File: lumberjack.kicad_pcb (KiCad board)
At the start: 2 copper layers, 285.4 x 94.9 mm, 151 parts, among them J1 USB_OTG, J2 AVR_ISP_6, SW1 RESET, SW2 BOOT, U1 ATMEGA328-PU, Y1 16MHz

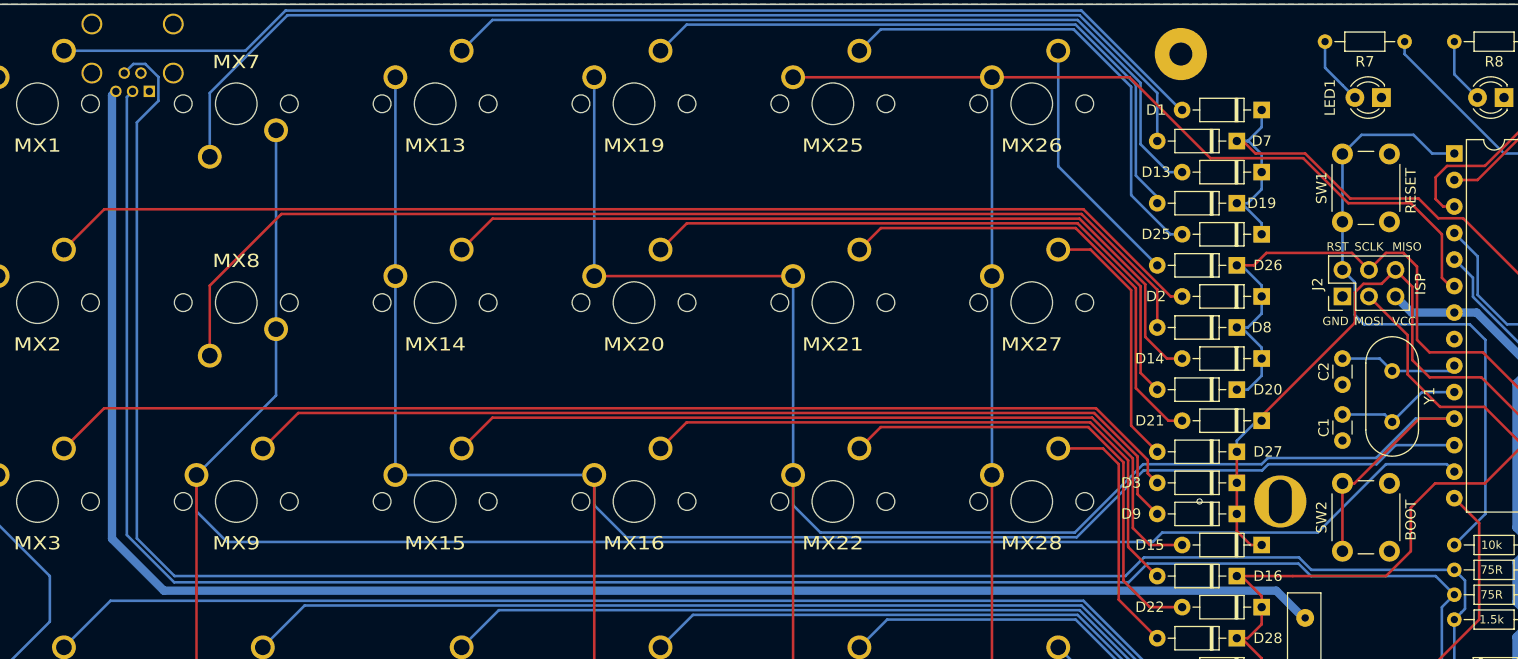
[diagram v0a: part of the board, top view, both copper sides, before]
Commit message: Add JST socket footprint for USB daughterboard
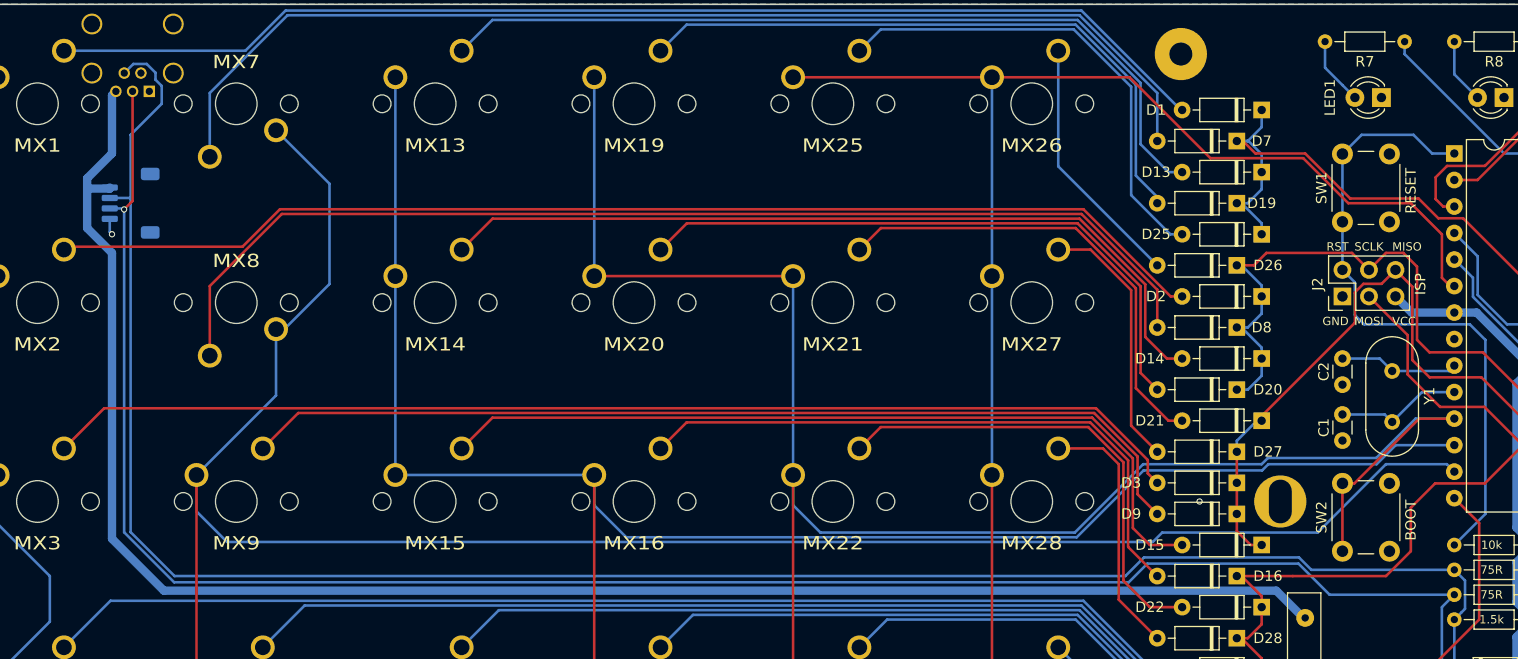
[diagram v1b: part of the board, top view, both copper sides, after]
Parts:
- added J3: JST, Connector_JST:JST_SH_SM04B-SRSS-TB_1x04-1MP_P1.00mm_Horizontal, B.Cu at (28.0, 73.8)
- added REF**: OSHW-Logo2_9.8x8mm_Copper, Symbol:OSHW-Logo2_9.8x8mm_Copper, B.Cu at (147.6, 116.1)
- J1: value USB_OTG -> USB
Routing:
- net /COL1: track 221.9 -> 226.6 mm
- net Net-(F1-Pad1): track 160.5 -> 164.8 mm
- net Net-(D67-Pad1): track 188.6 -> 191.4 mm
- net Net-(D66-Pad1): track 185.0 -> 186.6 mm, vias 0 -> 1
- net GND: track 0.00 -> 1.57 mm, vias 3 -> 4
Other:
- rule pad_to_mask_clearance: 0.2 -> 0
- board text added: "Lumberjack rev1.2 u/peejeh 01/2021"
- board text removed: "Lumberjack rev1.1 u/peejeh 12/2020"

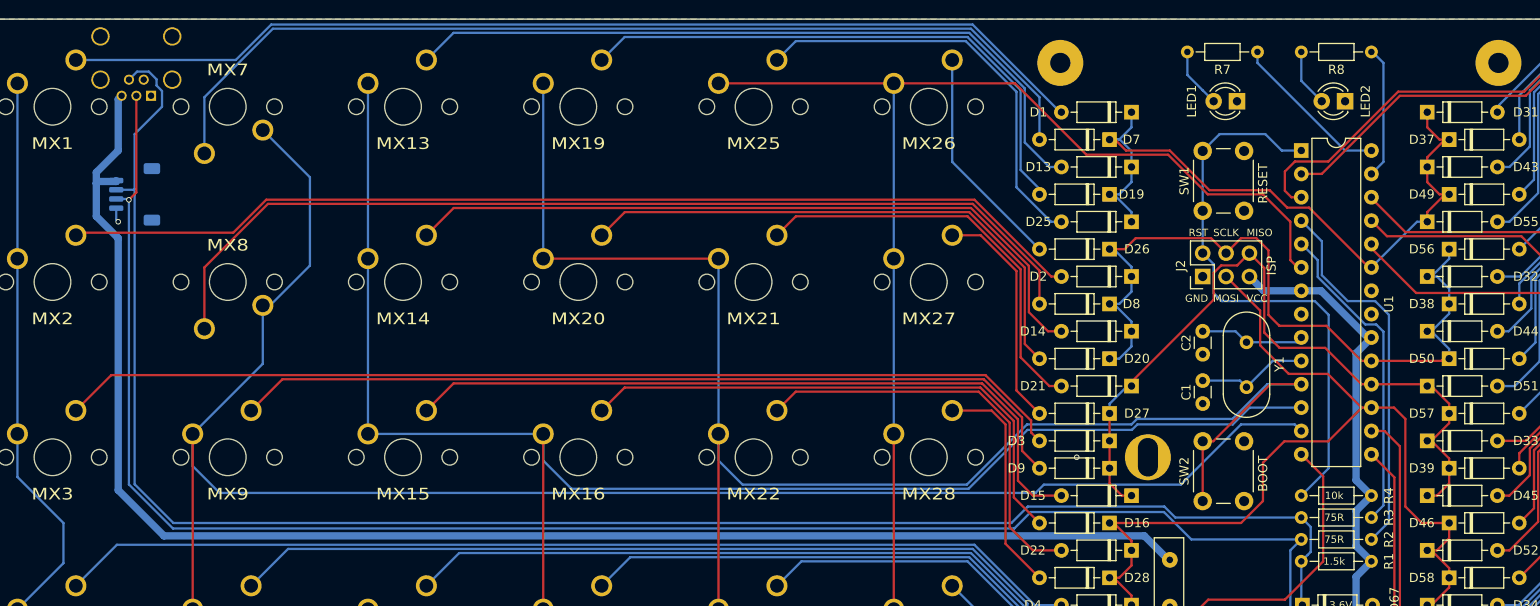
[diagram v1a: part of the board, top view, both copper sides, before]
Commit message: Add optional USB-C connector and resistors
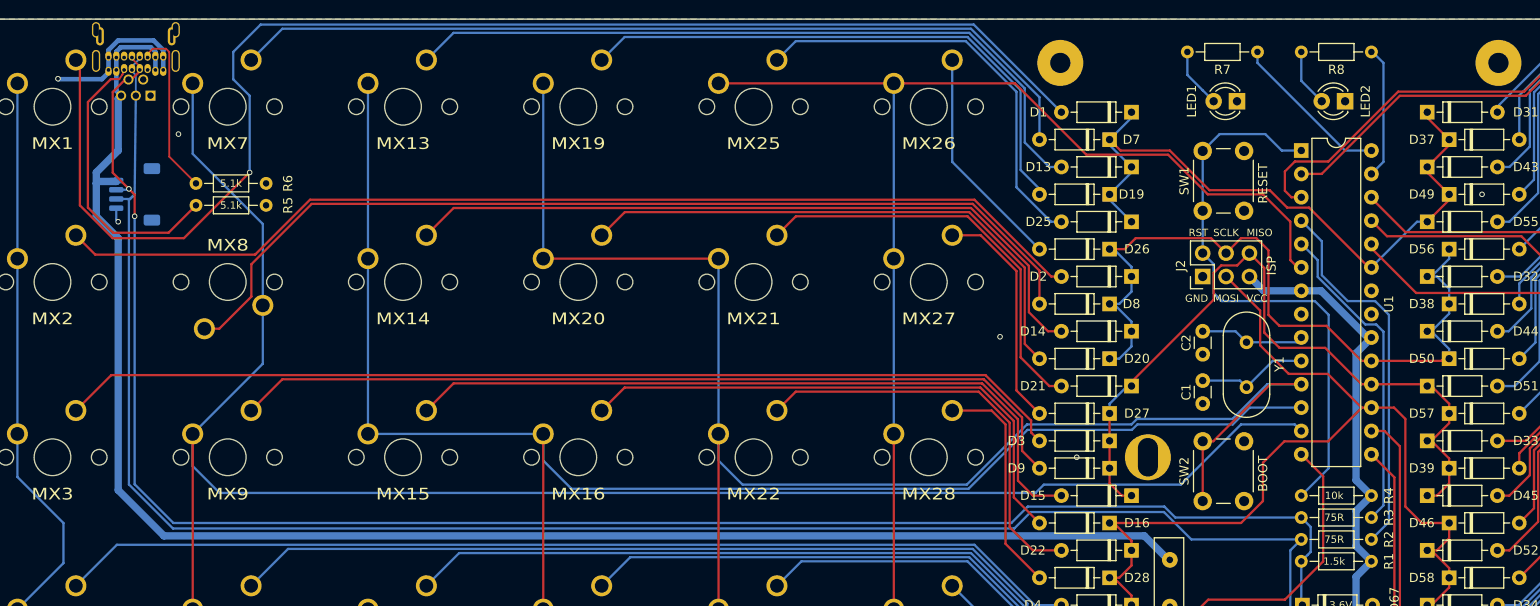
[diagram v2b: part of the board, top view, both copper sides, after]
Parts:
- removed the REF** at (147.6, 116.1)
- added R5: 5.1k, Resistor_THT:R_Axial_DIN0204_L3.6mm_D1.6mm_P7.62mm_Horizontal, F.Cu at (42.3, 75.0)
- added R6: 5.1k, Resistor_THT:R_Axial_DIN0204_L3.6mm_D1.6mm_P7.62mm_Horizontal, F.Cu at (42.3, 72.6)
- added REF**: OSHW-Logo_7.5x8mm_Copper, Symbol:OSHW-Logo_7.5x8mm_Copper, B.Cu at (147.6, 116.7)
- J1: footprint lumberjack:USB_Mini-B -> lumberjack:USB_Hybrid_THT
- moved R2 7.62 mm to (154.8, 111.3), turned to 0 degrees
- moved R3 7.62 mm to (154.8, 108.9), turned to 0 degrees
- moved J1 5.41 mm to (25.1, 60.3), turned to 0 degrees
- turned MX7 to 0 degrees
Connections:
- R2 pad 1: /USB_D+ -> Net-(D66-Pad1)
- R2 pad 2: Net-(D66-Pad1) -> /USB_D+
- R3 pad 1: /USB_D- -> Net-(D67-Pad1)
- R3 pad 2: Net-(D67-Pad1) -> /USB_D-
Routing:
- net Net-(D1-Pad2): track 112.7 -> 147.9 mm, vias 0 -> 1
- net Net-(J1-PadCC1): track 0.00 -> 31.2 mm
- net Net-(J1-PadCC2): track 0.00 -> 18.8 mm
- net GND: track 1.57 -> 18.8 mm, vias 4 -> 8
- net Net-(D7-Pad2): track 107.7 -> 94.8 mm
- net Net-(F1-Pad1): track 164.8 -> 176.4 mm
- net Net-(D66-Pad1): track 186.6 -> 192.2 mm, vias 1 -> 0
- net /COL1: track 226.6 -> 230.1 mm
- net /ROW0: track 77.4 -> 74.0 mm
- net Net-(D8-Pad2): track 106.9 -> 105.1 mm
- net Net-(D2-Pad2): track 112.2 -> 113.9 mm
- net Net-(D67-Pad1): track 191.4 -> 191.1 mm, vias 0 -> 2
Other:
- board text added: "Lumberjack rev1.3 u/peejeh 02/2021"
- board text removed: "Lumberjack rev1.2 u/peejeh 01/2021"

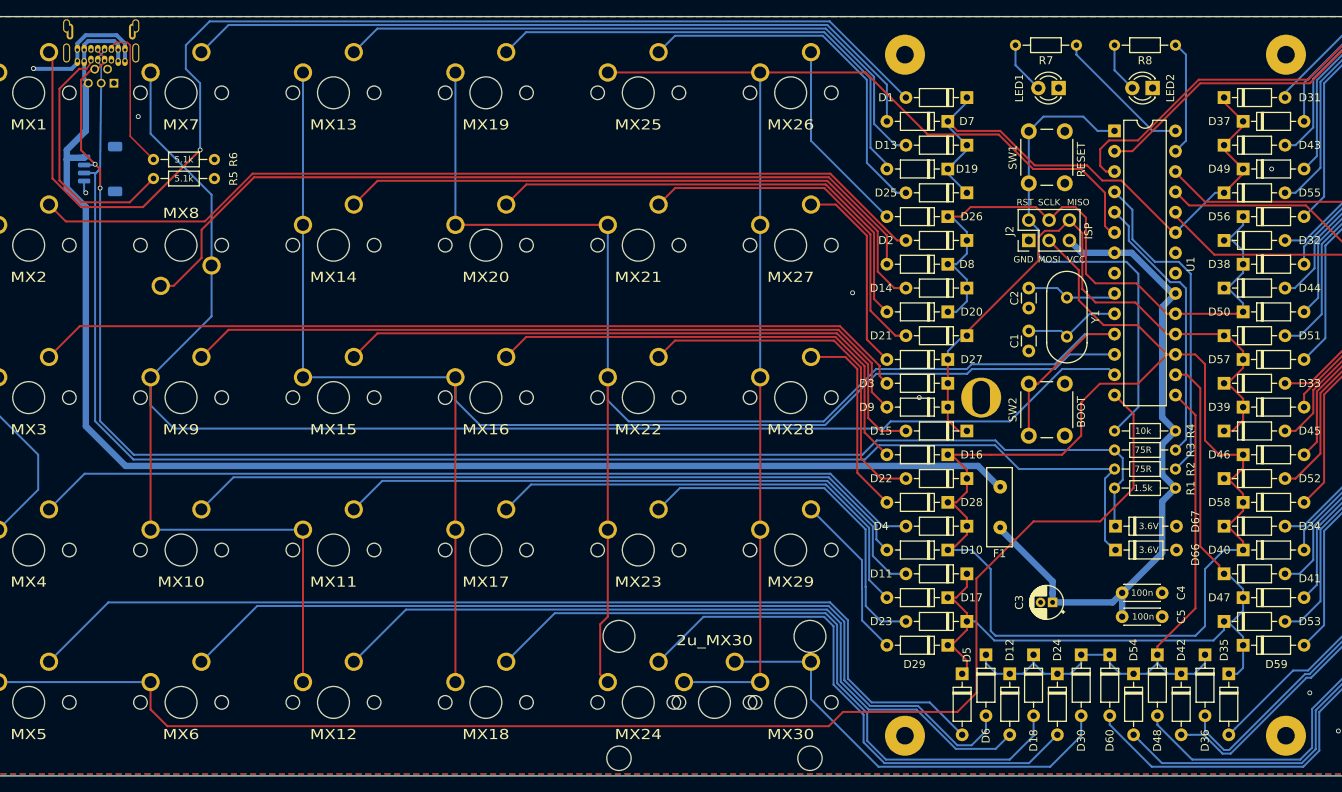
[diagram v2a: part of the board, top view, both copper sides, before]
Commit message: Move USB-C resistors to top row
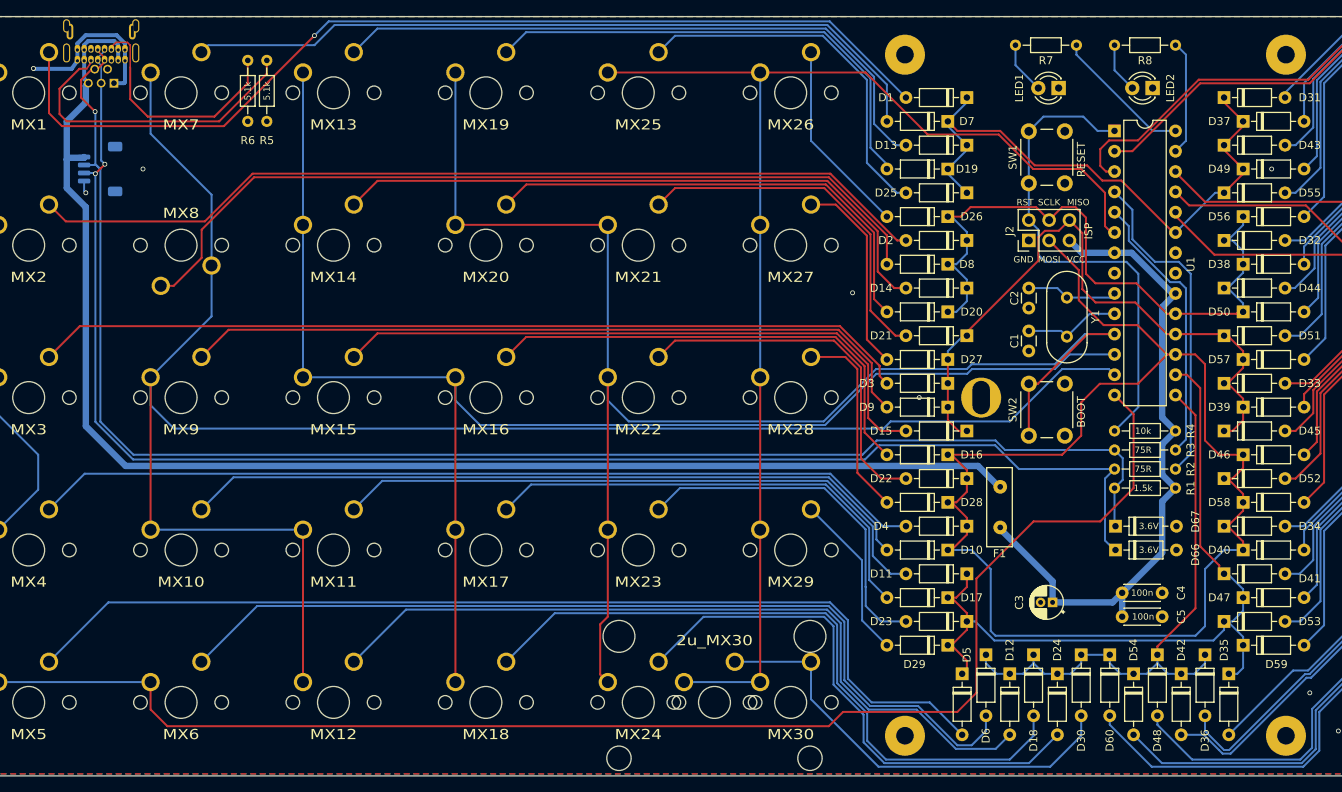
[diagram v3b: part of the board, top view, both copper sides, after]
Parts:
- moved R5 9.69 mm to (48.8, 67.9), turned to 90 degrees
- moved R6 6.33 mm to (46.4, 67.9), turned to 90 degrees
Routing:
- net Net-(D1-Pad2): track 147.9 -> 124.8 mm
- net Net-(J1-PadCC2): track 18.8 -> 30.2 mm
- net Net-(J1-PadCC1): track 31.2 -> 39.2 mm
- net GND: track 18.8 -> 22.8 mm
- net Net-(D67-Pad1): track 191.1 -> 191.9 mm, vias 2 -> 1
- net Net-(D66-Pad1): track 192.2 -> 191.8 mm, vias 0 -> 2

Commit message: Update signature silk
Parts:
- added REF**: flags, lumberjack:Flags, B.Cu at (240.9, 146.7)
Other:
- board text added: "Lumberjack rev1.3 u/peejeh 03/2021"
- board text removed: "Lumberjack rev1.3 u/peejeh 02/2021"

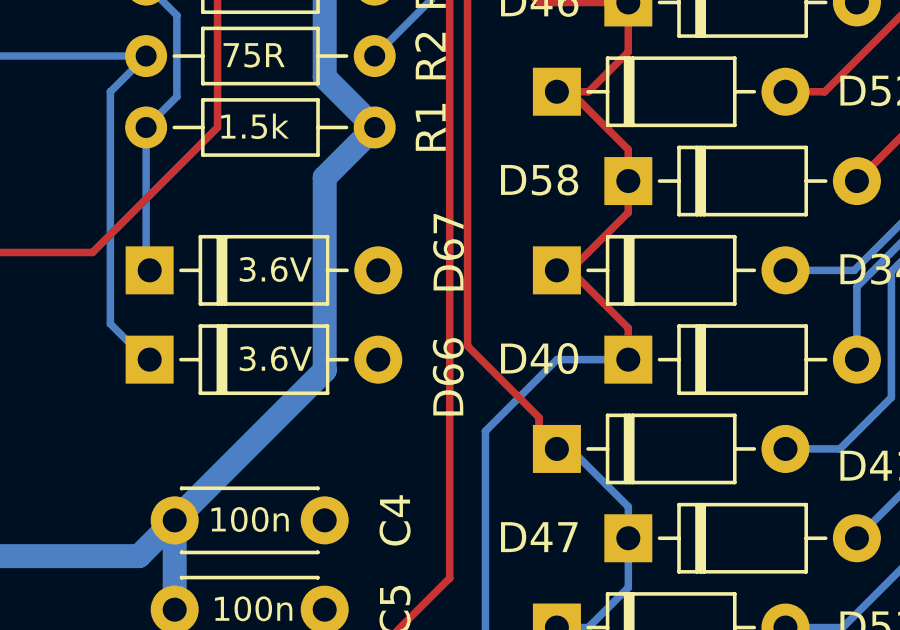
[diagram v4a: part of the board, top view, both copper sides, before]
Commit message: Fix naming of zener diode footprints
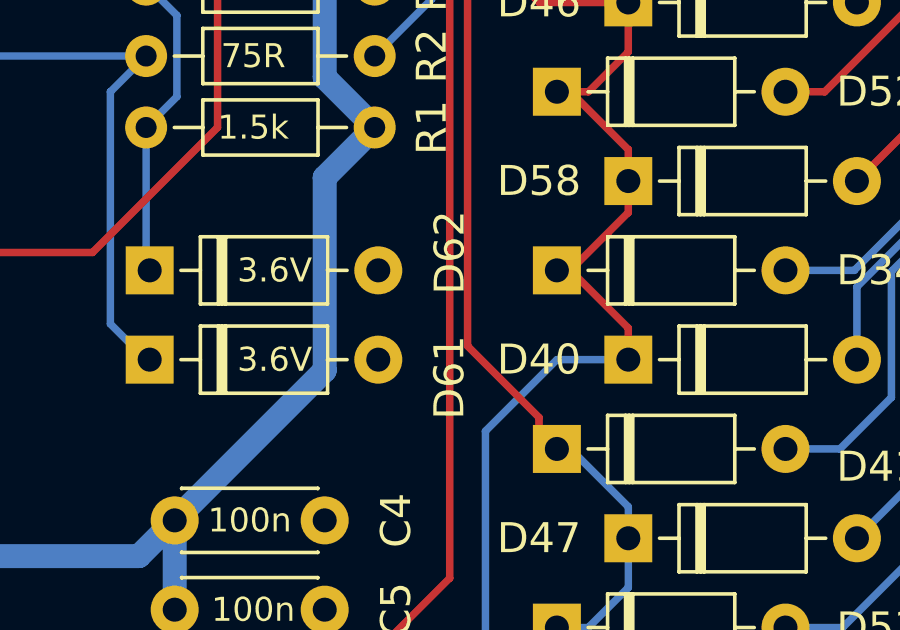
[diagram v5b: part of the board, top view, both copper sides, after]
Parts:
- renumbered D66 to D61, D67 to D62

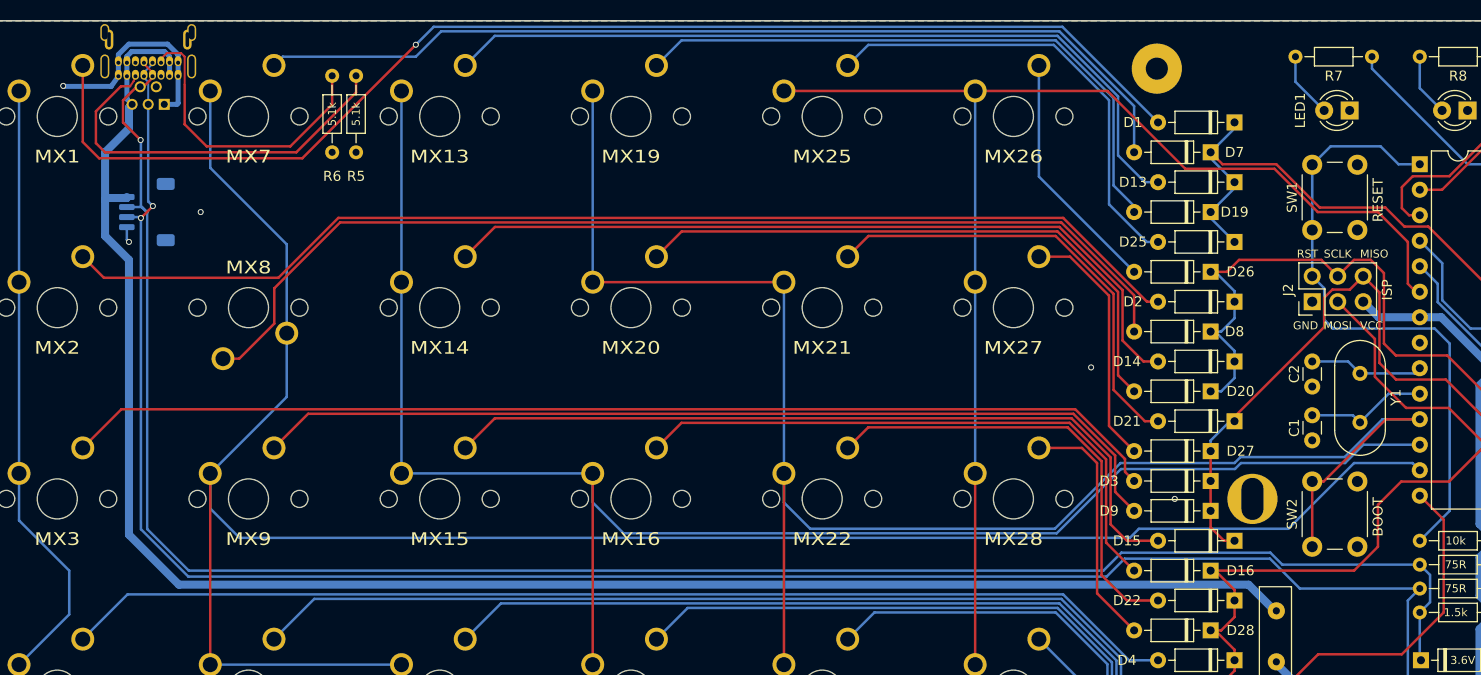
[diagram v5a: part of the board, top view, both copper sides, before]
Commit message: Use USB footprint with better positioning
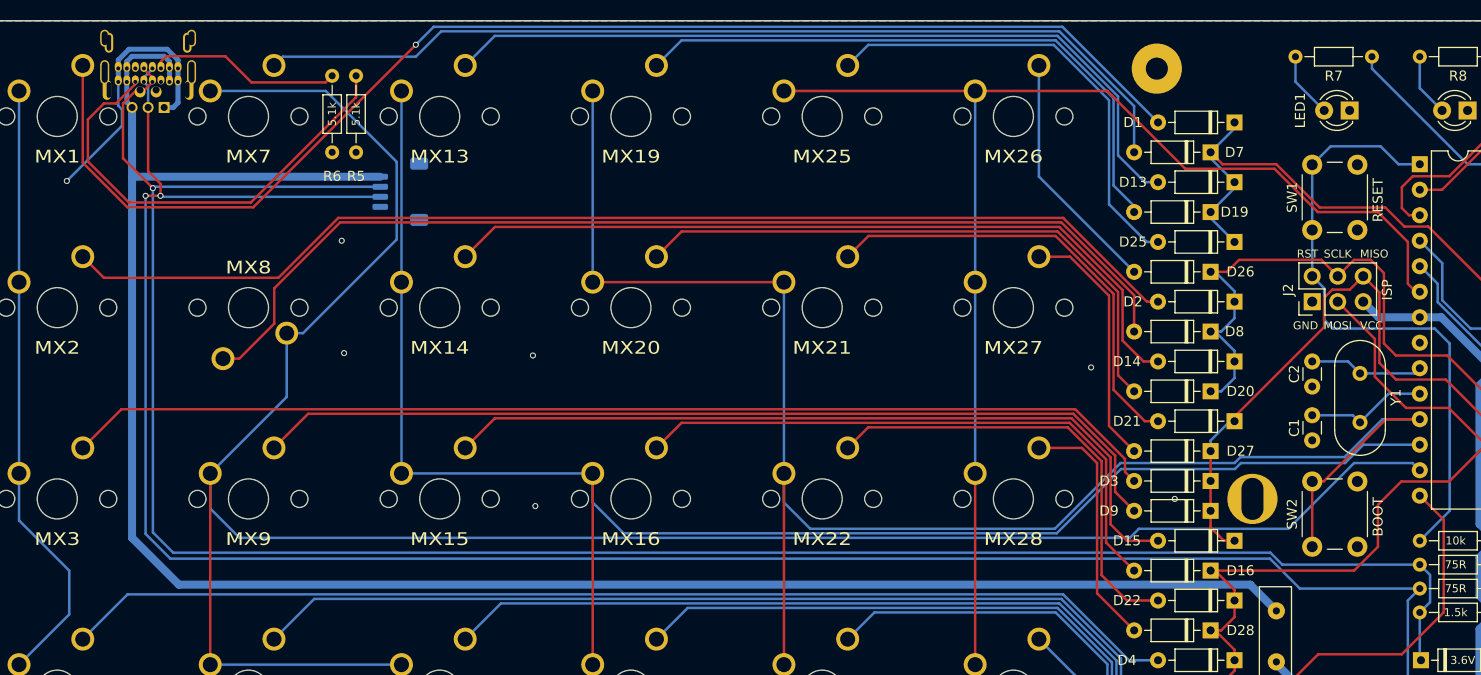
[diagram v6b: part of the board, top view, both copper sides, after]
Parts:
- J1: footprint lumberjack:USB_Hybrid_THT -> lumberjack:USB_Hybrid
- moved J3 25.3 mm to (53.2, 71.8)
- moved J1 0.56 mm to (25.1, 60.9)
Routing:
- net Net-(F1-Pad1): track 176.4 -> 196.2 mm
- net Net-(D66-Pad1): track 191.8 -> 211.2 mm
- net Net-(D67-Pad1): track 191.9 -> 210.3 mm
- net /COL1: track 230.1 -> 246.9 mm
- net Net-(J1-PadCC2): track 30.2 -> 19.3 mm
- net Net-(J1-PadCC1): track 39.2 -> 46.0 mm
- net Net-(D1-Pad2): track 124.8 -> 130.0 mm
- net GND: track 22.8 -> 27.1 mm, vias 8 -> 10
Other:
- board text added: "Lumberjack rev1.4 u/peejeh 10/2021"
- board text removed: "Lumberjack rev1.3 u/peejeh 03/2021"
